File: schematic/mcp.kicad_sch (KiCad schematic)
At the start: 13 parts, among them U2 MC9S12ZVL

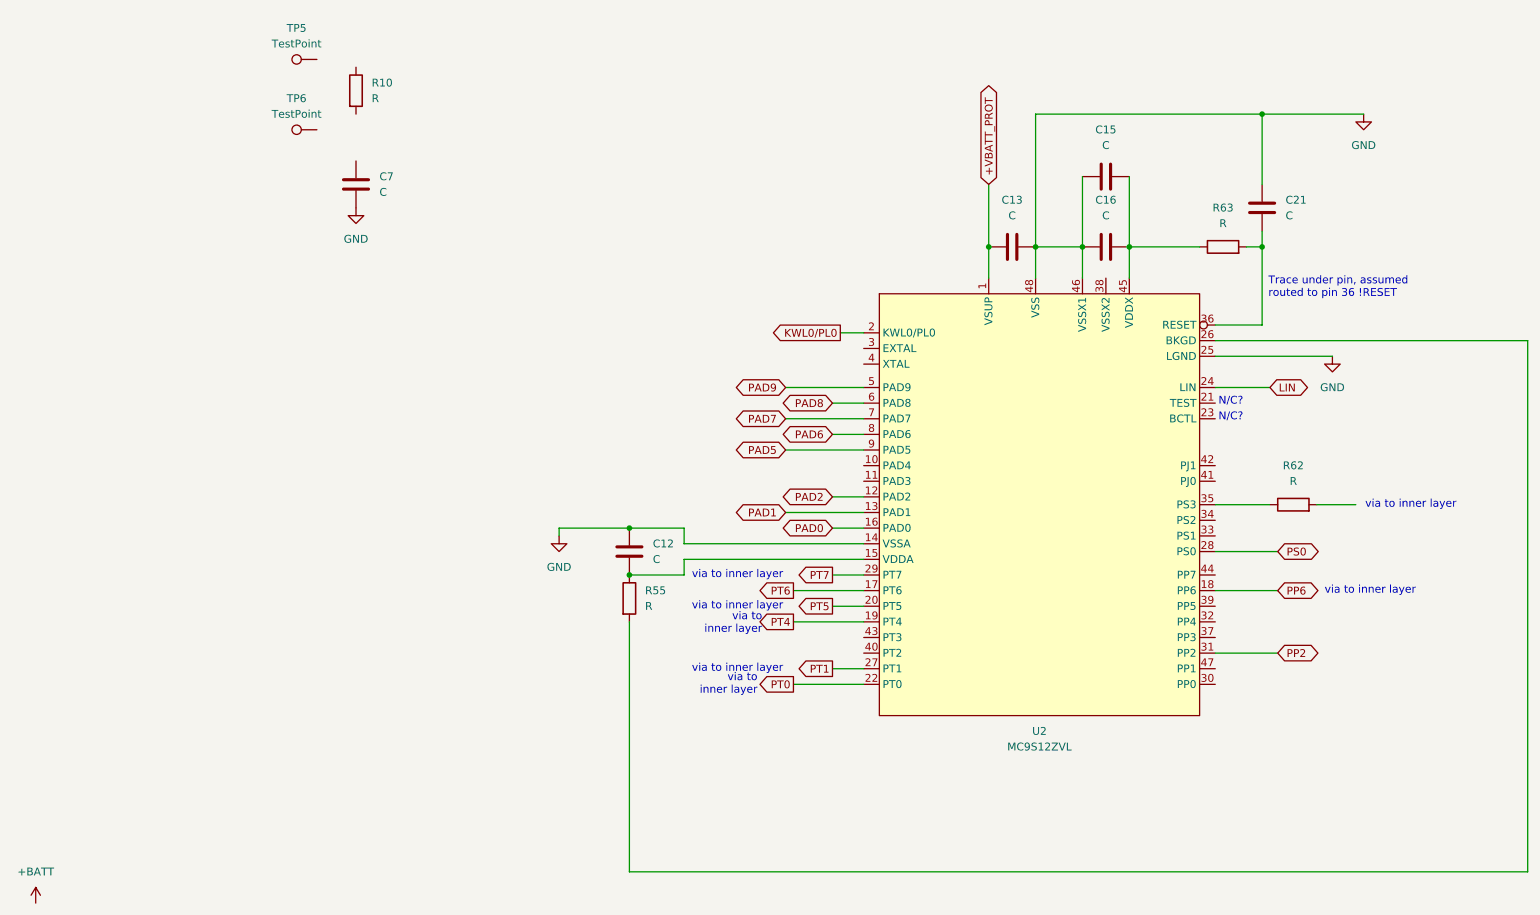
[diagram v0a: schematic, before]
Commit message: Added J5 and assoc. resistor network. Added traceable signals for MYSTERY_SIG
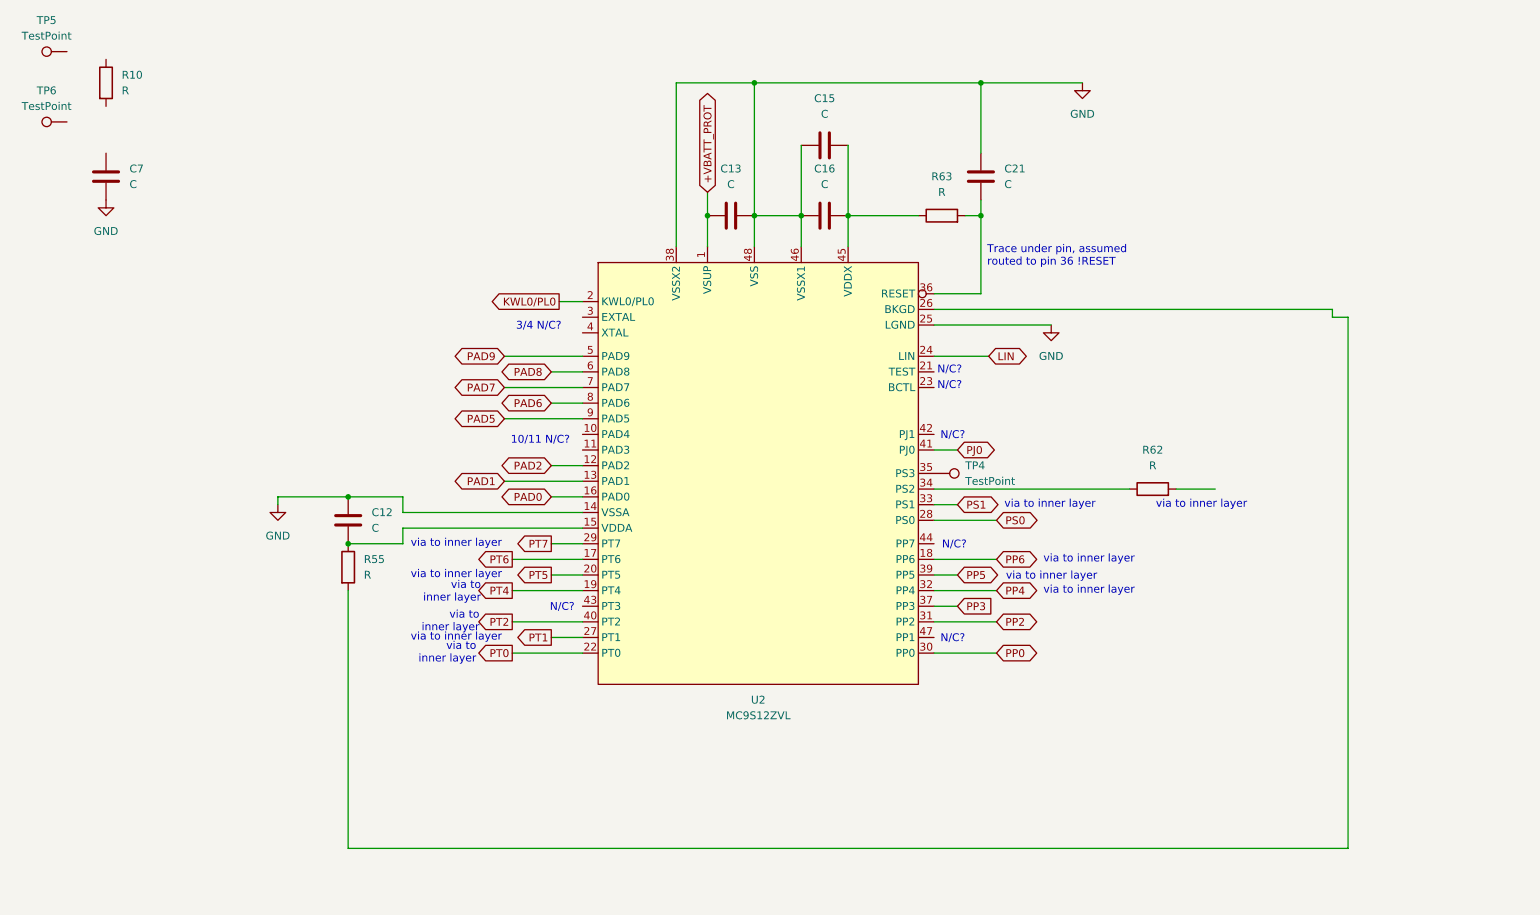
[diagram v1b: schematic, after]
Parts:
- added TP4: TestPoint, symbol Connector:TestPoint
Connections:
- net GND: now also U2.38 (VSSX2)
- net PP0: now reaches U2.30 (PP0)
- net PP4: now reaches U2.32 (PP4)
- net PS1: now reaches U2.33 (PS1)
- net at U2.34 (PS2): now also R62.1
- net at U2.35 (PS3): now also TP4.1; no longer R62.1
- net PP3: now reaches U2.37 (PP3)
- net PP5: now reaches U2.39 (PP5)
- net PT2: now reaches U2.40 (PT2)
- net PJ0: now reaches U2.41 (PJ0)
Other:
- note added: "10/11 N/C?"
- note added: "3/4 N/C?"
- moved on the sheet: C12, C13, C15, C16, C21, C7, R10, R55, R62, R63, TP5, TP6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
